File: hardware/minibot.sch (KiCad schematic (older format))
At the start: 38 parts, among them J1 USB_OTG, J2 RESET, J3 CONN_01X18, J4 BAUD, J5 SWD, SW1 BOOT, SW2 RESET, U1 LSM6DS3US, U2 TLV70233DBV, U3 RN41

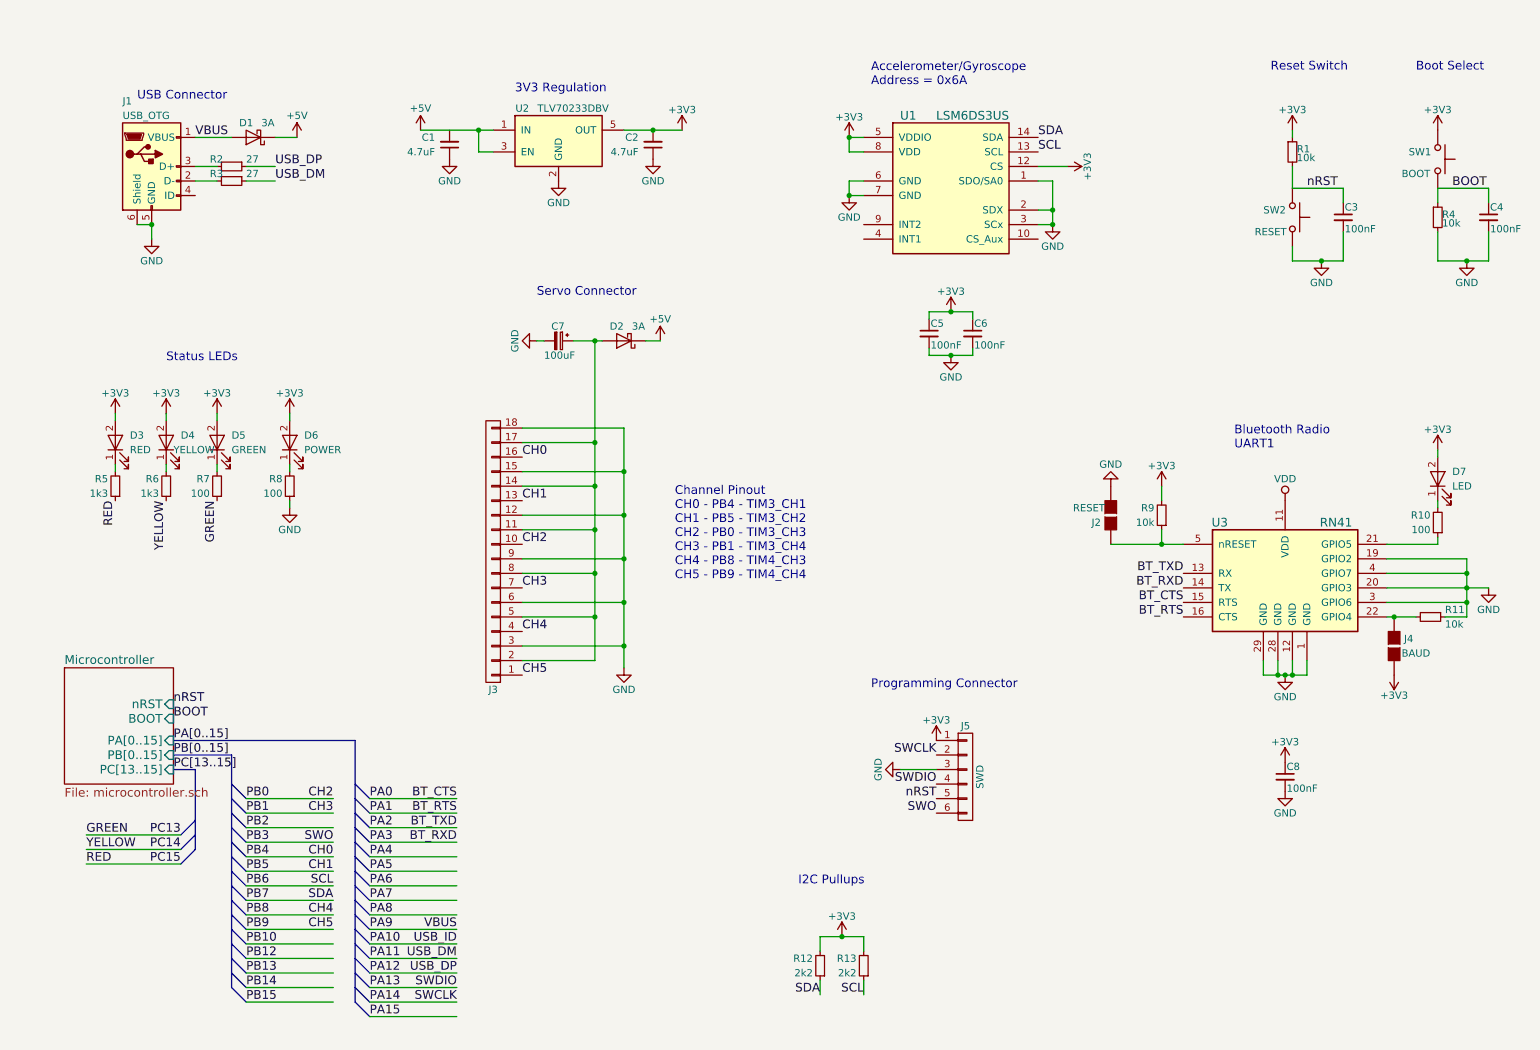
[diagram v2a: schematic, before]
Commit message: Redo the pinout. Plot the PDF. Layout the rest of the board.
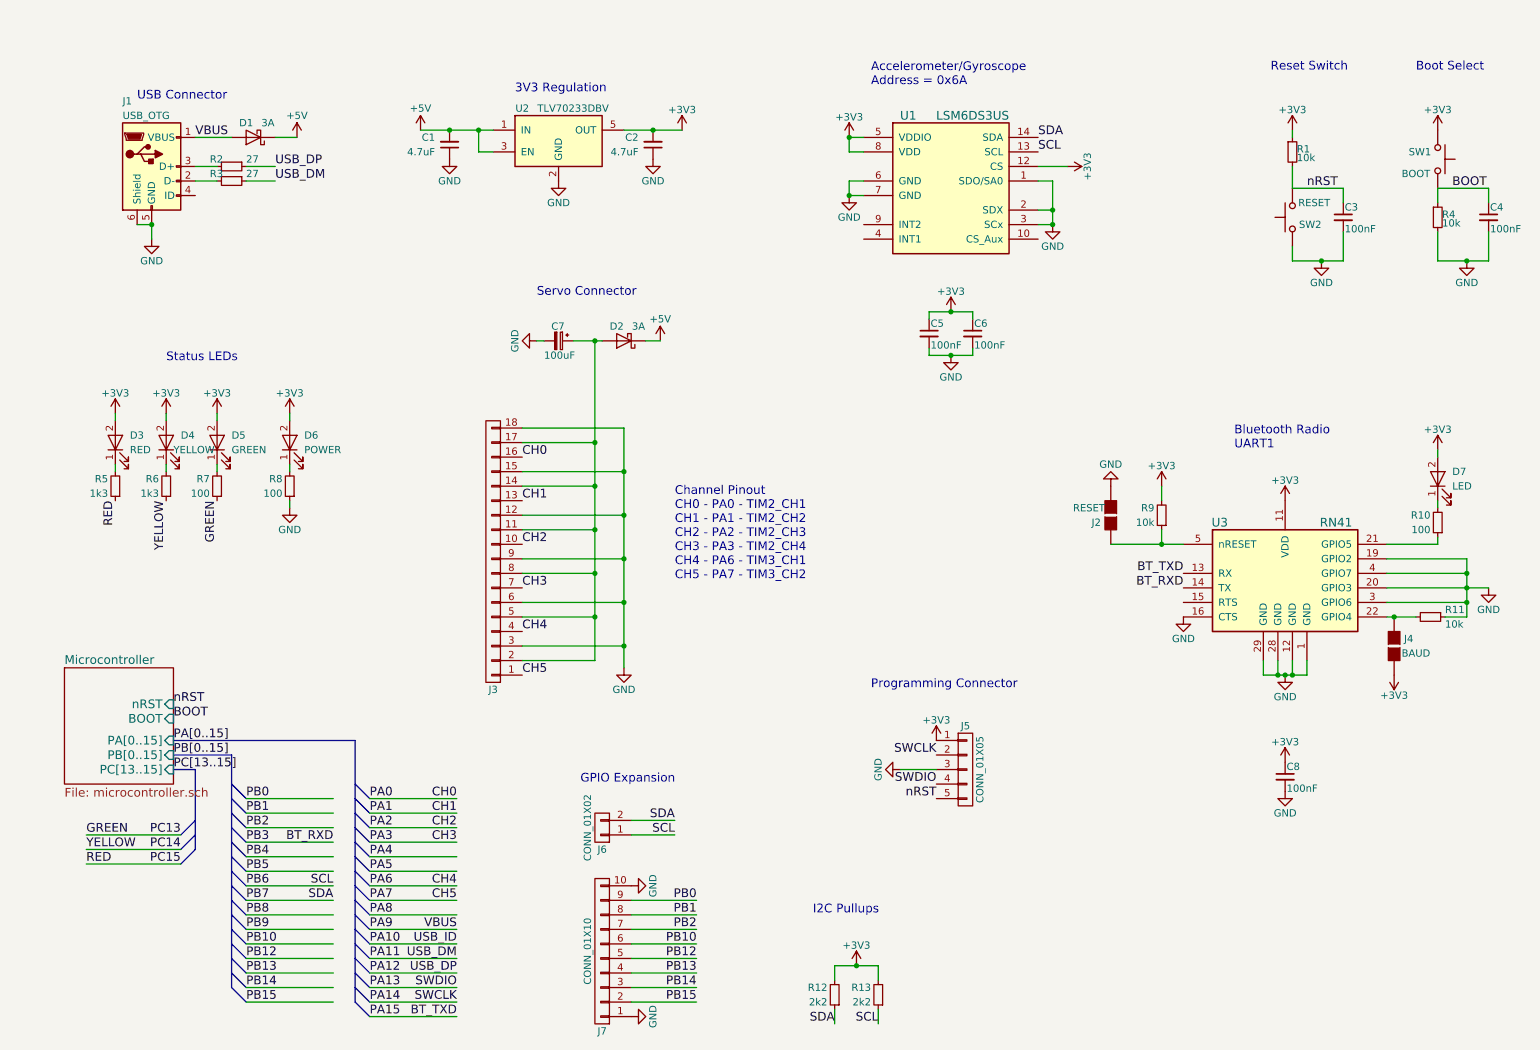
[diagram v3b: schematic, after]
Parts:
- removed J5: SWD, Pin_Headers:Pin_Header_Straight_1x06_Pitch1.27mm, symbol CONN_01X06
- added J5: CONN_01X05, Pin_Headers:Pin_Header_Angled_1x05_Pitch2.54mm, symbol CONN_01X05
- added J6: CONN_01X02, Pin_Headers:Pin_Header_Straight_1x02_Pitch2.54mm, symbol CONN_01X02
- added J7: CONN_01X10, Pin_Headers:Pin_Header_Straight_1x10_Pitch2.54mm, symbol CONN_01X10
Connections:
- net labels removed: BT_CTS, BT_RTS, SWO, VDD
- wire segments 128 -> 138
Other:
- note added: "Channel Pinout\nCH0 - PA0 - TIM2_CH1\nCH1 - PA1 - TIM2_CH2\nCH2 - PA2 - TIM2_CH3\nCH3 - PA3 - TIM2_CH4\nCH4 - PA6 - TIM3_CH1\nCH5 - PA7 - TIM3_CH2"
- note added: "GPIO Expansion"
- note removed: "Channel Pinout\nCH0 - PB4 - TIM3_CH1\nCH1 - PB5 - TIM3_CH2\nCH2 - PB0 - TIM3_CH3\nCH3 - PB1 - TIM3_CH4\nCH4 - PB8 - TIM4_CH3\nCH5 - PB9 - TIM4_CH4"
- moved on the sheet: R12, R13, SW2
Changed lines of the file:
@@
 F 3 "" H 9450 2150 50  0001 C CNN
 	1    9450 1950
-	0    1    1    0
+	0    -1   -1   0
 $EndComp
 $Comp
@@
 F 3 "" H 9400 5100 50  0001 C CNN
 	1    9400 5100
-	1    0    0    -1
-$EndComp
-$Comp
-L VDD #PWR05
-U 1 1 5943A32B
-P 9400 3900
-F 0 "#PWR05" H 9400 3750 50  0001 C CNN
-F 1 "VDD" H 9400 4050 50  0000 C CNN
-F 2 "" H 9400 3900 50  0001 C CNN
-F 3 "" H 9400 3900 50  0001 C CNN
-	1    9400 3900
 	1    0    0    -1
 $EndComp
@@
 Status LEDs\n
 $Comp
-L CONN_01X06 J5
-U 1 1 5943812A
-P 7200 5800
-F 0 "J5" H 7200 6150 50  0000 C CNN
-F 1 "SWD" V 7300 5800 50  0000 C CNN
-F 2 "Pin_Headers:Pin_Header_Straight_1x06_Pitch1.27mm" H 7200 5800 50  0001 C CNN
-F 3 "" H 7200 5800 50  0001 C CNN
-	1    7200 5800
-	1    0    0    -1
-$EndComp
-$Comp
 L GND #PWR016
 U 1 1 59438DDC
@@
 Text Label 7000 5950 2    60   ~ 0
 nRST
-Text Label 7000 6050 2    60   ~ 0
-SWO
 Text Notes 6550 5200 0    60   ~ 0
 Programming Connector
@@
 Text Label 3700 7350 2    60   ~ 0
 SWCLK
-Text Label 2850 6250 2    60   ~ 0
-SWO
 Text Label 2050 3900 3    60   ~ 0
 GREEN
@@
 Text Label 8700 4500 2    60   ~ 0
 BT_RXD
+Text Label 3700 7450 2    60   ~ 0
+BT_TXD
+Text Label 2850 6250 2    60   ~ 0
+BT_RXD
+Text Label 3700 5950 2    60   ~ 0
+CH0
+Text Label 3700 6050 2    60   ~ 0
+CH1
 Text Label 3700 6150 2    60   ~ 0
-BT_TXD
+CH2
 Text Label 3700 6250 2    60   ~ 0
-BT_RXD
-Text Label 2850 6350 2    60   ~ 0
-CH0
-Text Label 2850 6450 2    60   ~ 0
-CH1
-Text Label 2850 5950 2    60   ~ 0
-CH2
-Text Label 2850 6050 2    60   ~ 0
 CH3
-Text Label 2850 6750 2    60   ~ 0
+Text Label 3700 6550 2    60   ~ 0
 CH4
-Text Label 2850 6850 2    60   ~ 0
+Text Label 3700 6650 2    60   ~ 0
 CH5
 $Comp
@@
 Text Label 7700 1400 0    60   ~ 0
 SDA
-Text Label 6500 7300 2    60   ~ 0
+Text Label 6600 7500 2    60   ~ 0
 SCL
 Text Notes 6550 1050 0    60   ~ 0
@@
 Text Label 2850 6650 2    60   ~ 0
 SDA
-Text Label 6200 7300 2    60   ~ 0
+Text Label 6300 7500 2    60   ~ 0
 SDA
 Text Label 7700 1500 0    60   ~ 0
@@
 L R_Small R13
 U 1 1 5946DE00
-P 6500 7100
-F 0 "R13" H 6550 7050 50  0000 L CNN
-F 1 "2k2" H 6550 7150 50  0000 L CNN
-F 2 "Resistors_SMD:R_0603" H 6500 7100 50  0001 C CNN
-F 3 "" H 6500 7100 50  0001 C CNN
-	1    6500 7100
+P 6600 7300
+F 0 "R13" H 6650 7250 50  0000 L CNN
+F 1 "2k2" H 6650 7350 50  0000 L CNN
+F 2 "Resistors_SMD:R_0603" H 6600 7300 50  0001 C CNN
+F 3 "" H 6600 7300 50  0001 C CNN
+	1    6600 7300
 	-1   0    0    1
 $EndComp
@@
 L R_Small R12
 U 1 1 5946DF2C
-P 6200 7100
-F 0 "R12" H 6250 7050 50  0000 L CNN
-F 1 "2k2" H 6250 7150 50  0000 L CNN
-F 2 "Resistors_SMD:R_0603" H 6200 7100 50  0001 C CNN
-F 3 "" H 6200 7100 50  0001 C CNN
-	1    6200 7100
-	-1   0    0    1
-$EndComp
-Wire Wire Line
-	6200 6900 6200 7000
-Wire Wire Line
-	6500 6900 6500 7000
-Wire Wire Line
-	6500 7300 6500 7200
-Wire Wire Line
-	6200 7300 6200 7200
-Text Notes 6050 6550 0    60   ~ 0
+P 6300 7300
+F 0 "R12" H 6350 7250 50  0000 L CNN
+F 1 "2k2" H 6350 7350 50  0000 L CNN
+F 2 "Resistors_SMD:R_0603" H 6300 7300 50  0001 C CNN
+F 3 "" H 6300 7300 50  0001 C CNN
+	1    6300 7300
+	-1   0    0    1
+$EndComp
+Wire Wire Line
+	6300 7100 6300 7200
+Wire Wire Line
+	6600 7100 6600 7200
+Wire Wire Line
+	6600 7500 6600 7400
+Wire Wire Line
+	6300 7500 6300 7400
+Text Notes 6150 6750 0    60   ~ 0
 I2C Pullups\n
 Wire Wire Line
-	6200 6900 6500 6900
-Connection ~ 6350 6900
+	6300 7100 6600 7100
+Connection ~ 6450 7100
 $Comp
 L C_Small C8
@@
 	3450 1350 3950 1350
 Text Notes 5200 4450 0    60   ~ 0
-Channel Pinout\nCH0 - PB4 - TIM3_CH1\nCH1 - PB5 - TIM3_CH2\nCH2 - PB0 - TIM3_CH3\nCH3 - PB1 - TIM3_CH4\nCH4 - PB8 - TIM4_CH3\nCH5 - PB9 - TIM4_CH4
+Channel Pinout\nCH0 - PA0 - TIM2_CH1\nCH1 - PA1 - TIM2_CH2\nCH2 - PA2 - TIM2_CH3\nCH3 - PA3 - TIM2_CH4\nCH4 - PA6 - TIM3_CH1\nCH5 - PA7 - TIM3_CH2
 $Comp
 L +3V3 #PWR022
@@
 L +3V3 #PWR030
 U 1 1 5948FF64
-P 6350 6900
-F 0 "#PWR030" H 6350 6750 50  0001 C CNN
-F 1 "+3V3" H 6350 7040 50  0000 C CNN
-F 2 "" H 6350 6900 50  0001 C CNN
-F 3 "" H 6350 6900 50  0001 C CNN
-	1    6350 6900
+P 6450 7100
+F 0 "#PWR030" H 6450 6950 50  0001 C CNN
+F 1 "+3V3" H 6450 7240 50  0000 C CNN
+F 2 "" H 6450 7100 50  0001 C CNN
+F 3 "" H 6450 7100 50  0001 C CNN
+	1    6450 7100
 	1    0    0    -1
 $EndComp
@@
 	1    0    0    -1
 $EndComp
-Text Label 8700 4600 2    60   ~ 0
-BT_CTS
-Text Label 8700 4700 2    60   ~ 0
-BT_RTS
-Text Label 3700 5950 2    60   ~ 0
-BT_CTS
-Text Label 3700 6050 2    60   ~ 0
-BT_RTS
 Text Label 1750 5550 0    60   ~ 0
 PA[0..15]
@@
 Text Label 2250 7350 0    60   ~ 0
 PB15
+$Comp
+L CONN_01X05 J5
+U 1 1 5951AE21
+P 7200 5750
+F 0 "J5" H 7200 6050 50  0000 C CNN
+F 1 "CONN_01X05" V 7300 5750 50  0000 C CNN
+F 2 "Pin_Headers:Pin_Header_Angled_1x05_Pitch2.54mm" H 7200 5750 50  0001 C CNN
+F 3 "" H 7200 5750 50  0001 C CNN
+	1    7200 5750
+	1    0    0    -1
+$EndComp
+$Comp
+L GND #PWR038
+U 1 1 5951BF73
+P 8700 4700
+F 0 "#PWR038" H 8700 4450 50  0001 C CNN
+F 1 "GND" H 8700 4550 50  0000 C CNN
+F 2 "" H 8700 4700 50  0001 C CNN
+F 3 "" H 8700 4700 50  0001 C CNN
+	1    8700 4700
+	1    0    0    -1
+$EndComp
+Connection ~ 3650 1350
+$Comp
+L CONN_01X10 J7
+U 1 1 5952347D
+P 4700 7000
+F 0 "J7" H 4700 7550 50  0000 C CNN
+F 1 "CONN_01X10" V 4800 7000 50  0000 C CNN
+F 2 "Pin_Headers:Pin_Header_Straight_1x10_Pitch2.54mm" H 4700 7000 50  0001 C CNN
+F 3 "" H 4700 7000 50  0001 C CNN
+	1    4700 7000
+	-1   0    0    1
+$EndComp
+$Comp
+L GND #PWR039
+U 1 1 5952375D
+P 4900 7450
+F 0 "#PWR039" H 4900 7200 50  0001 C CNN
+F 1 "GND" H 4900 7300 50  0000 C CNN
+F 2 "" H 4900 7450 50  0001 C CNN
+F 3 "" H 4900 7450 50  0001 C CNN
+	1    4900 7450
+	0    -1   -1   0
+$EndComp
+$Comp
+L GND #PWR040
+U 1 1 595237FB
+P 4900 6550
+F 0 "#PWR040" H 4900 6300 50  0001 C CNN
+F 1 "GND" H 4900 6400 50  0000 C CNN
+F 2 "" H 4900 6550 50  0001 C CNN
+F 3 "" H 4900 6550 50  0001 C CNN
+	1    4900 6550
+	0    -1   -1   0
+$EndComp
+Wire Wire Line
+	4900 6650 5350 6650
+Wire Wire Line
+	4900 6750 5350 6750
+Wire Wire Line
+	5350 6850 4900 6850
+Wire Wire Line
+	4900 6950 5350 6950
+Wire Wire Line
+	5350 7050 4900 7050
+Wire Wire Line
+	4900 7150 5350 7150
+Wire Wire Line
+	5350 7250 4900 7250
+Wire Wire Line
+	4900 7350 5350 7350
+Text Label 5350 6650 2    60   ~ 0
+PB0
+Text Label 5350 6750 2    60   ~ 0
+PB1
+Text Label 5350 6850 2    60   ~ 0
+PB2
+Text Label 5350 6950 2    60   ~ 0
+PB10
+Text Label 5350 7050 2    60   ~ 0
+PB12
+Text Label 5350 7150 2    60   ~ 0
+PB13
+Text Label 5350 7250 2    60   ~ 0
+PB14
+Text Label 5350 7350 2    60   ~ 0
+PB15
+$Comp
+L CONN_01X02 J6
+U 1 1 59524F61
+P 4700 6150
+F 0 "J6" H 4700 6300 50  0000 C CNN
+F 1 "CONN_01X02" V 4800 6150 50  0000 C CNN
+F 2 "Pin_Headers:Pin_Header_Straight_1x02_Pitch2.54mm" H 4700 6150 50  0001 C CNN
+F 3 "" H 4700 6150 50  0001 C CNN
+	1    4700 6150
+	-1   0    0    1
+$EndComp
+Wire Wire Line
+	4900 6100 5200 6100
+Wire Wire Line
+	4900 6200 5200 6200
+Text Label 5200 6100 2    60   ~ 0
+SDA
+Text Label 5200 6200 2    60   ~ 0
+SCL
+Text Notes 4550 5850 0    60   ~ 0
+GPIO Expansion
+$Comp
+L +3V3 #PWR?
+U 1 1 59527FD5
+P 9400 3900
+F 0 "#PWR?" H 9400 3750 50  0001 C CNN
+F 1 "+3V3" H 9400 4040 50  0000 C CNN
+F 2 "" H 9400 3900 50  0001 C CNN
+F 3 "" H 9400 3900 50  0001 C CNN
+	1    9400 3900
+	1    0    0    -1
+$EndComp
 $EndSCHEMATC

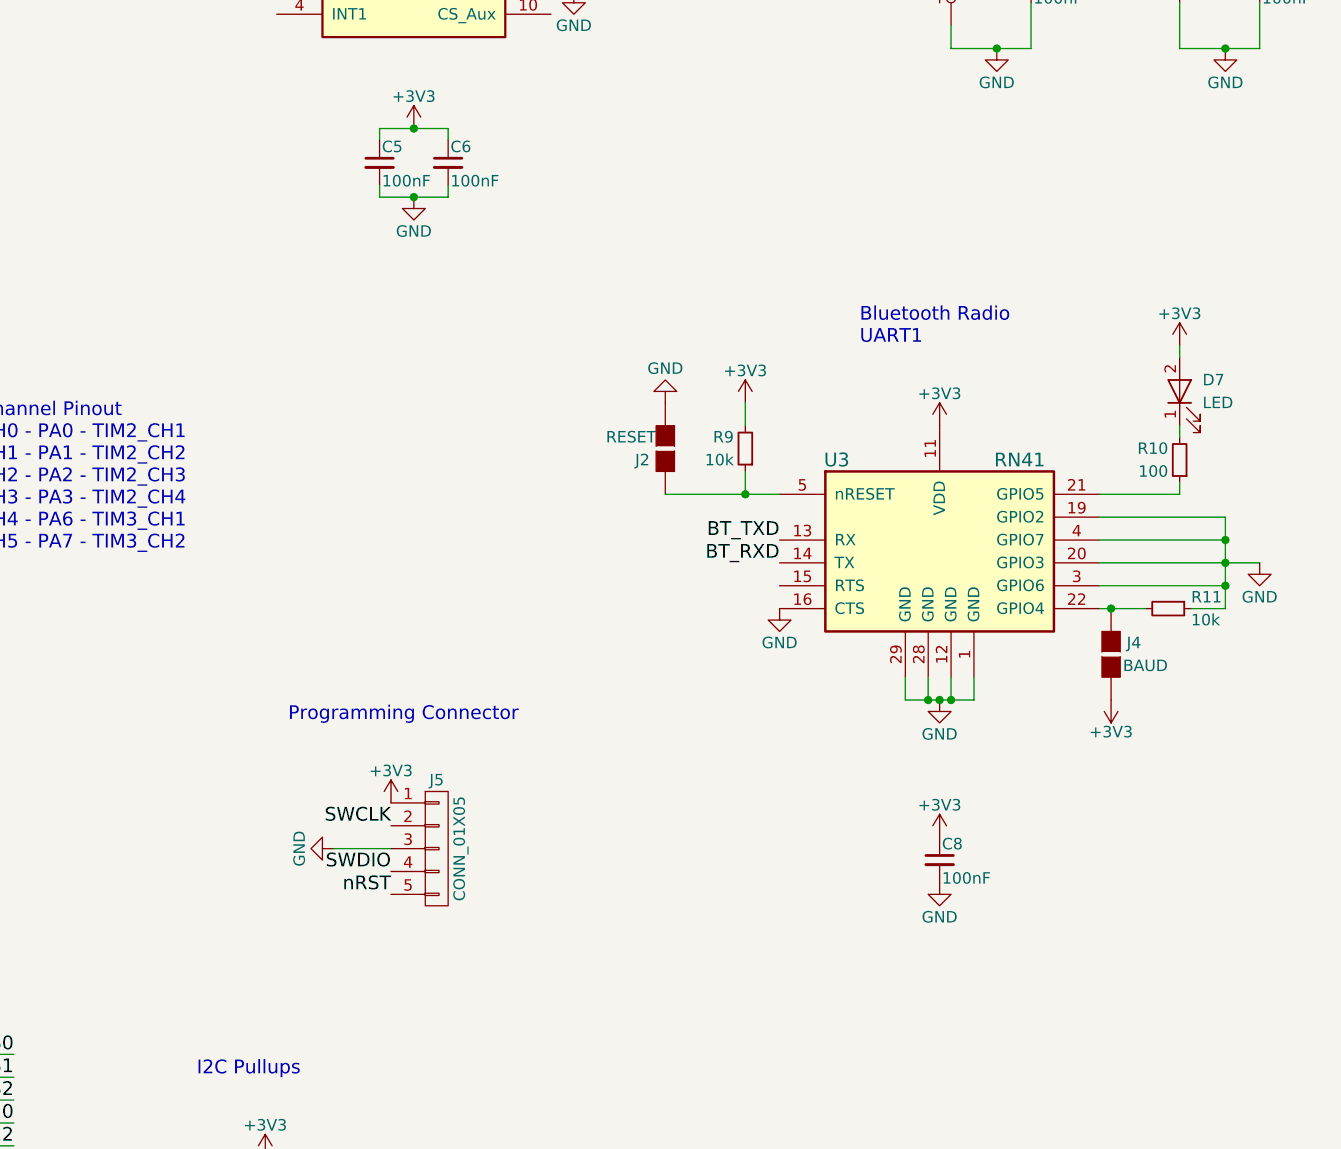
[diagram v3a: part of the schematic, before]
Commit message: Tweak the layout a little bit. Add mounting holes and some pads to solder the power leads onto.
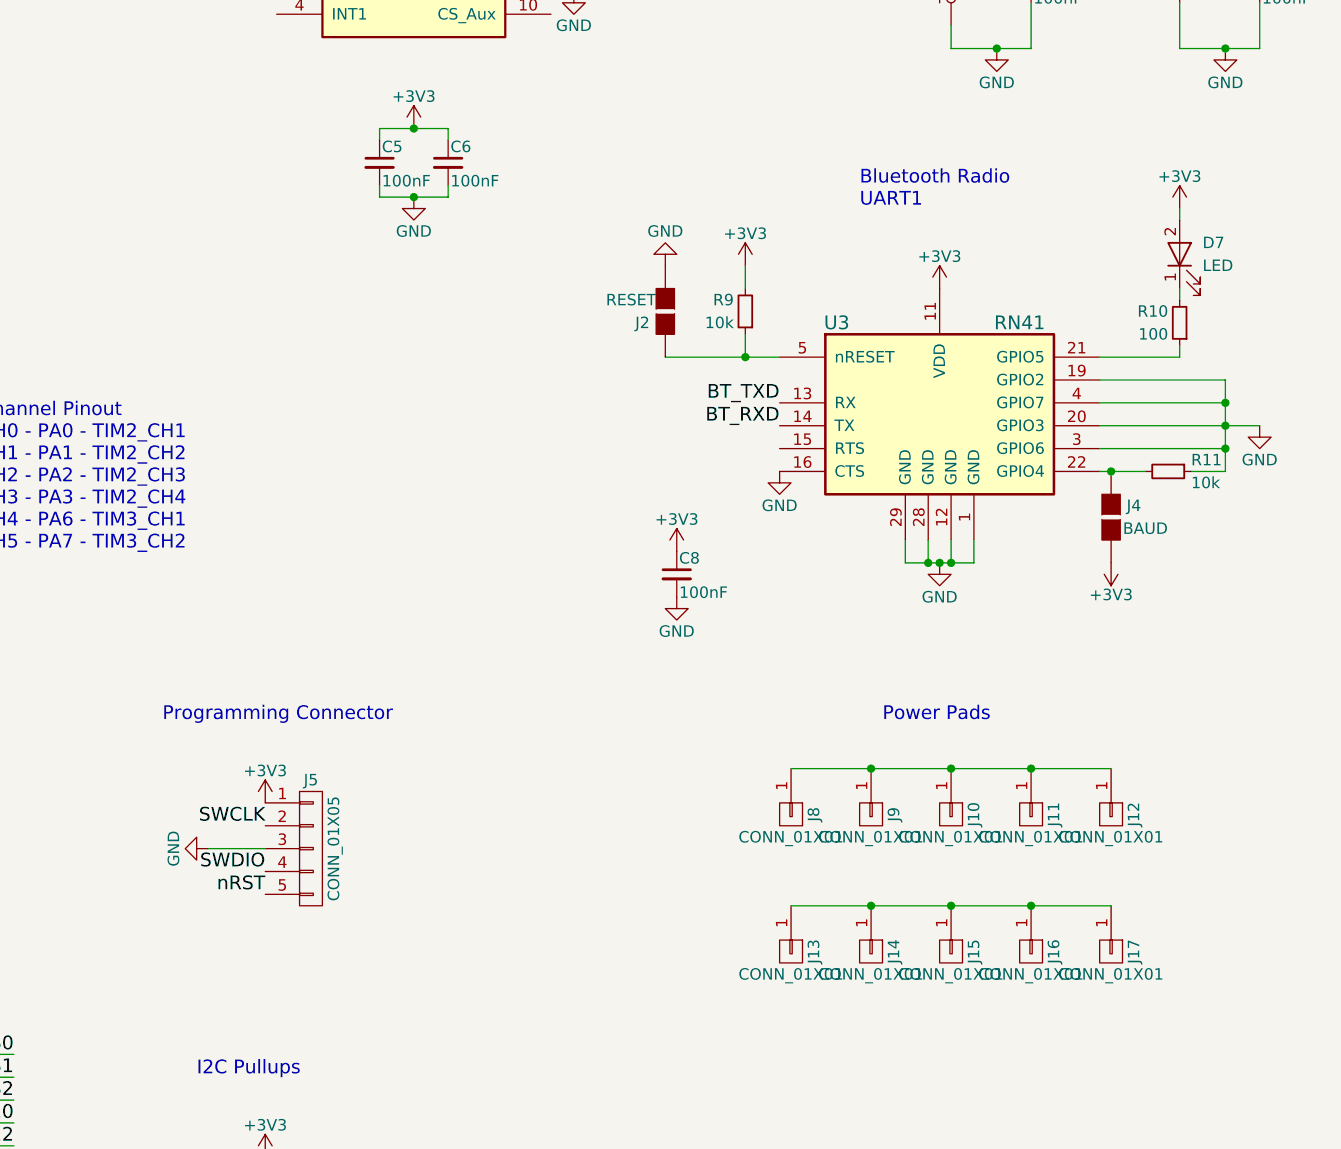
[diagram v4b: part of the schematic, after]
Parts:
- added J10, J11, J12, J13, J14, J15, J16, J17, J8, J9: CONN_01X01, parts:Pad, symbol CONN_01X01
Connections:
- wire segments 138 -> 140
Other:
- note added: "Power Pads"
- moved on the sheet: C8, D7, J2, J4, J5, R10, R11, R9, U3
